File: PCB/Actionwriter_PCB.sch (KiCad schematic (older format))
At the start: 20 parts, among them J1 Conn_01x01, U1 74HC595, U2 74HC595

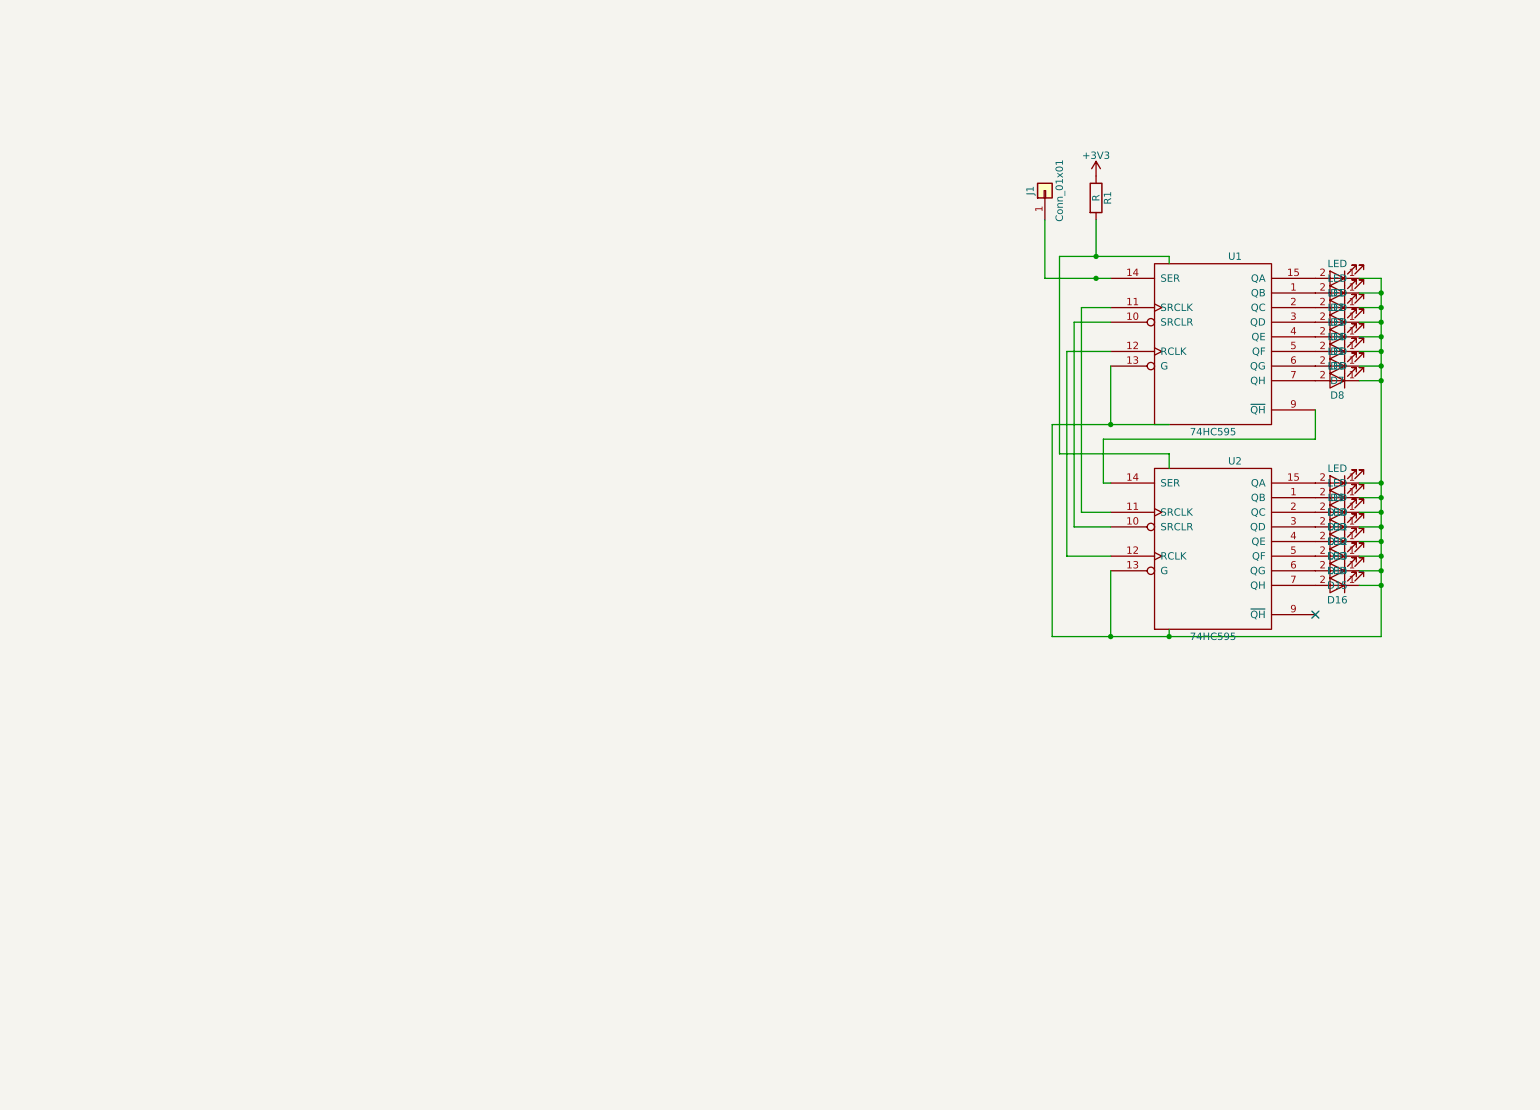
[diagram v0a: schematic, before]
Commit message: Schematic seems finished
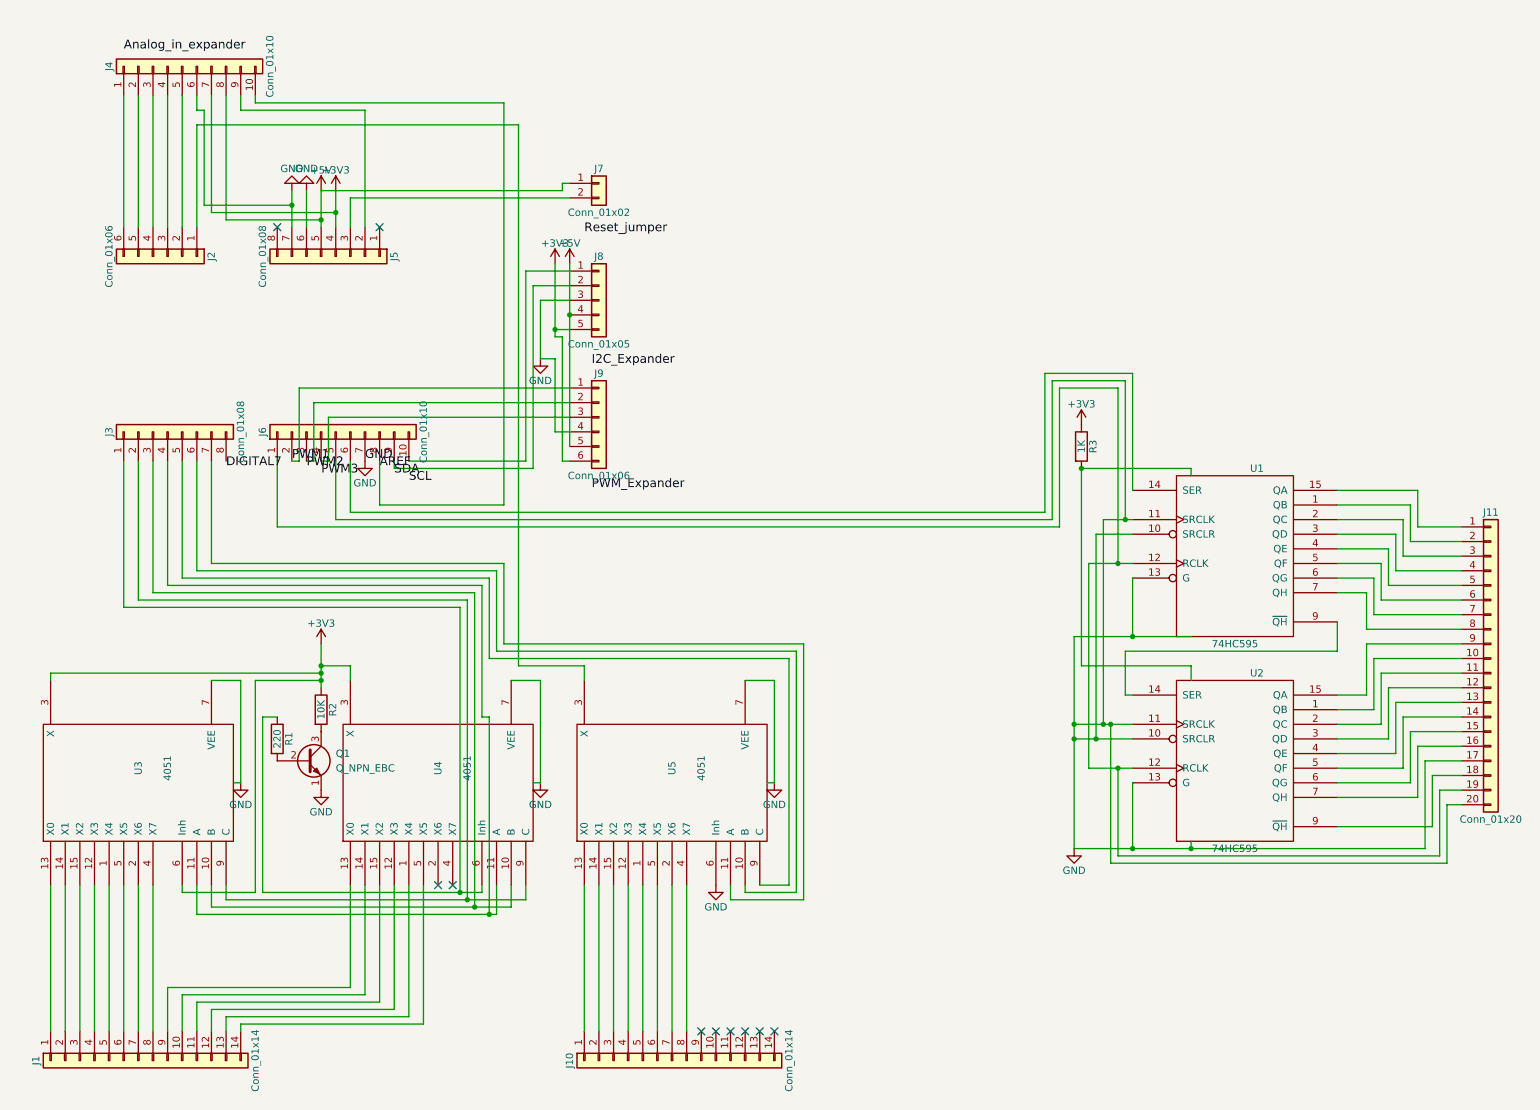
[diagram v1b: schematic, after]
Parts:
- removed D1, D10, D11, D12, D13, D14, D15, D16, D2, D3, D4, D5, D6, D7, D8, D9: LED, LEDs:LED_D5.0mm, symbol LED
- removed J1: Conn_01x01, Pin_Headers:Pin_Header_Straight_1x01_Pitch1.00mm, symbol Conn_01x01
- added J1, J10: Conn_01x14, Pin_Headers:Pin_Header_Straight_1x14_Pitch2.54mm, symbol Conn_01x14
- added J11: Conn_01x20, Pin_Headers:Pin_Header_Straight_1x20_Pitch2.54mm, symbol Conn_01x20
- added J2, J9: Conn_01x06, Pin_Headers:Pin_Header_Straight_1x06_Pitch2.54mm, symbol Conn_01x06
- added J3, J5: Conn_01x08, Pin_Headers:Pin_Header_Straight_1x08_Pitch2.54mm, symbol Conn_01x08
- added J4, J6: Conn_01x10, Pin_Headers:Pin_Header_Straight_1x10_Pitch2.54mm, symbol Conn_01x10
- added J7: Conn_01x02, Pin_Headers:Pin_Header_Straight_1x02_Pitch2.54mm, symbol Conn_01x02
- added J8: Conn_01x05, Pin_Headers:Pin_Header_Straight_1x05_Pitch2.54mm, symbol Conn_01x05
- added Q1: Q_NPN_EBC, Transistors_OldSowjetAera:OldSowjetaera_Transistor_Type-II_SmallPads, symbol Q_NPN_EBC
- added R2: 10K, Resistors_SMD:R_1206_HandSoldering, symbol R
- added R3: 1K, Resistors_SMD:R_1206_HandSoldering, symbol R
- added U3, U4, U5: 4051, Housings_DIP:DIP-16_W7.62mm, symbol 4051
- R1: value R -> 220; footprint Resistors_SMD:R_0805_HandSoldering -> Resistors_SMD:R_1206_HandSoldering
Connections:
- net +3V3: now also J4.7 (Pin_7), J5.4 (Pin_4), J8.5 (Pin_5), J9.6 (Pin_6), R2.1, R3.1, U3.3 (X), U3.6 (Inh), U4.3 (X); no longer R1.1
- net GND: now also U1.10 (SRCLR), U1.11 (SRCLK), U2.10 (SRCLR), U2.11 (SRCLK), J11.17 (Pin_17), J11.20 (Pin_20), J4.6 (Pin_6), J5.6 (Pin_6), J5.7 (Pin_7), J6.5 (Pin_5), J6.7 (Pin_7), J8.3 (Pin_3), J9.4 (Pin_4), Q1.1 (E), U3.7 (VEE), U3.8 (VSS), U4.7 (VEE), U4.8 (VSS), U5.6 (Inh), U5.7 (VEE), U5.8 (VSS)
- net VCC: now also R3.2; no longer R1.2
- net at U1.1 (QB): now also J11.2 (Pin_2)
- net at U1.12 (RCLK), U2.12 (RCLK): now also J11.19 (Pin_19), J6.1 (Pin_1)
- net at U1.14 (SER): now also J6.6 (Pin_6)
- net at U1.15 (QA): now also J11.1 (Pin_1)
- net at U1.2 (QC): now also J11.3 (Pin_3)
- net at U1.3 (QD): now also J11.4 (Pin_4)
- net at U1.4 (QE): now also J11.5 (Pin_5)
- net at U1.5 (QF): now also J11.6 (Pin_6)
- net at U1.6 (QG): now also J11.7 (Pin_7)
- net at U1.7 (QH): now also J11.8 (Pin_8)
- net at U2.1 (QB): now also J11.10 (Pin_10)
- net at U2.15 (QA): now also J11.9 (Pin_9)
- net at U2.2 (QC): now also J11.11 (Pin_11)
- net at U2.3 (QD): now also J11.12 (Pin_12)
- net at U2.4 (QE): now also J11.13 (Pin_13)
- net at U2.5 (QF): now also J11.14 (Pin_14)
- net at U2.6 (QG): now also J11.15 (Pin_15)
- net at U2.7 (QH): now also J11.16 (Pin_16)
- net at U2.9 (~QH): now also J11.18 (Pin_18)
- new net: J1.1 (Pin_1), U3.13 (X0)
- new net: J1.10 (Pin_10), U4.14 (X1)
- new net: J1.11 (Pin_11), U4.15 (X2)
- new net: J1.12 (Pin_12), U4.12 (X3)
- new net: J1.13 (Pin_13), U4.1 (X4)
- new net: J1.14 (Pin_14), U4.5 (X5)
- new net: J1.2 (Pin_2), U3.14 (X1)
- new net: J1.3 (Pin_3), U3.15 (X2)
- new net: J1.4 (Pin_4), U3.12 (X3)
- new net: J1.5 (Pin_5), U3.1 (X4)
- new net: J1.6 (Pin_6), U3.5 (X5)
- new net: J1.7 (Pin_7), U3.2 (X6)
- new net: J1.8 (Pin_8), U3.4 (X7)
- new net: J1.9 (Pin_9), U4.13 (X0)
- new net: J10.1 (Pin_1), U5.13 (X0)
- new net: J10.2 (Pin_2), U5.14 (X1)
- new net: J10.3 (Pin_3), U5.15 (X2)
- new net: J10.4 (Pin_4), U5.12 (X3)
- new net: J10.5 (Pin_5), U5.1 (X4)
- new net: J10.6 (Pin_6), U5.5 (X5)
- new net: J10.7 (Pin_7), U5.2 (X6)
- new net: J10.8 (Pin_8), U5.4 (X7)
- new net: J3.3 (Pin_3), U3.10 (B), U4.10 (B)
- new net: J3.4 (Pin_4), U3.11 (A), U4.11 (A)
- new net: J3.2 (Pin_2), U3.9 (C), U4.9 (C)
- new net: J3.1 (Pin_1), R1.1, U4.6 (Inh)
- new net: J3.6 (Pin_6), U5.10 (B)
- new net: J3.7 (Pin_7), U5.11 (A)
- new net: J2.1 (Pin_1), U5.3 (X)
- new net: J3.5 (Pin_5), U5.9 (C)
- new net: Q1.2 (B), R1.2
- new net: Q1.3 (C), R2.2
- new net: J6.10 (Pin_10), J8.1 (Pin_1)
- new net: J6.3 (Pin_3), J9.2 (Pin_2)
- new net: J6.4 (Pin_4), J9.3 (Pin_3)
- new net: J6.9 (Pin_9), J8.2 (Pin_2)
- new net: J4.9 (Pin_9), J5.2 (Pin_2)
- new net: J5.3 (Pin_3), J7.2 (Pin_2)
- new net: J2.2 (Pin_2), J4.5 (Pin_5)
- new net: J2.3 (Pin_3), J4.4 (Pin_4)
- new net: J2.4 (Pin_4), J4.3 (Pin_3)
- new net: J2.5 (Pin_5), J4.2 (Pin_2)
- new net: J2.6 (Pin_6), J4.1 (Pin_1)
- new net +5V: J4.8 (Pin_8), J5.5 (Pin_5), J7.1 (Pin_1), J8.4 (Pin_4), J9.5 (Pin_5)
- new net AREF: J4.10 (Pin_10), J6.8 (Pin_8)
- new net PWM1: J6.2 (Pin_2), J9.1 (Pin_1)
- new net VDD: U3.16 (VDD), U4.16 (VDD), U5.16 (VDD)
- no-connect marks 1 -> 10
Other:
- moved on the sheet: U1, U2

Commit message: Test moving some address lines to 0 and 1 (for later use of PWM), PCB work
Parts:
- removed J11: Conn_01x20, Pin_Headers:Pin_Header_Straight_1x20_Pitch2.54mm, symbol Conn_01x20
- removed J4: Conn_01x10, Pin_Headers:Pin_Header_Straight_1x10_Pitch2.54mm, symbol Conn_01x10
- removed Q1: Q_NPN_EBC, Transistors_OldSowjetAera:OldSowjetaera_Transistor_Type-II_SmallPads, symbol Q_NPN_EBC
- added J11: LEDS0, Pin_Headers:Pin_Header_Straight_1x09_Pitch2.54mm, symbol Conn_01x09
- added J12: LEDS1, Pin_Headers:Pin_Header_Straight_1x09_Pitch2.54mm, symbol Conn_01x09
- added J13: LEDX, Pin_Headers:Pin_Header_Straight_1x04_Pitch1.27mm_SMD_Pin1Right, symbol Conn_01x04
- added J4: AIN_D8_Expander, Pin_Headers:Pin_Header_Straight_1x11_Pitch2.54mm, symbol Conn_01x11
- added Q1: PN2222A, TO_SOT_Packages_THT:TO-92_Molded_Narrow, symbol PN2222A
- added Q2, Q3, Q4: IRLB8721PBF, TO_SOT_Packages_THT:TO-220-3_Vertical, symbol IRLB8721PBF
- J1: value Conn_01x14 -> KBD_LHS
- J10: value Conn_01x14 -> KBD_RHS; symbol Conn_01x14 -> Conn_01x16
- J2: value Conn_01x06 -> Arduino_AnalogIn
- J3: value Conn_01x08 -> Arduino_DigitalLow
- J5: value Conn_01x08 -> Arduino_power
- J6: value Conn_01x10 -> Arduino_DigitalHigh
- J7: value Conn_01x02 -> Reset_Jumper; footprint Pin_Headers:Pin_Header_Straight_1x02_Pitch2.54mm -> Pin_Headers:Pin_Header_Straight_1x03_Pitch2.54mm; symbol Conn_01x02 -> Conn_01x03
- J8: value Conn_01x05 -> I2C_Expander
- J9: value Conn_01x06 -> RGB_Expander
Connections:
- net VCC is gone; now on net +3V3: R3.2, U1.16 (VCC), U2.16 (VCC)
- net VDD is gone; now on net +3V3: U3.16 (VDD), U4.16 (VDD), U5.16 (VDD)
- net +3V3: now also J9.5 (Pin_5), J4.8 (Pin_8); no longer J9.6 (Pin_6)
- net +5V: now also J9.6 (Pin_6), J4.7 (Pin_7); no longer J7.1 (Pin_1), J9.5 (Pin_5)
- net AREF: now also J4.10 (Pin_10)
- net DIGITAL7: now also J3.8 (Pin_8), J4.11 (Pin_11)
- net GND: now also J7.1 (Pin_1), J11.1 (Pin_1), J12.9 (Pin_9), J13.2 (Pin_2), J13.4 (Pin_4), J4.6 (Pin_6), Q1.1 (E), Q2.3 (S), Q3.3 (S), Q4.3 (S); no longer J9.4 (Pin_4)
- net PWM1: now also Q2.1 (G); no longer J9.1 (Pin_1)
- net PWM2: now also J6.3 (Pin_3), Q3.1 (G)
- net PWM3: now also J6.4 (Pin_4), Q4.1 (G)
- net SCL: now also J6.10 (Pin_10), J8.1 (Pin_1)
- net SDA: now also J6.9 (Pin_9), J8.2 (Pin_2)
- net at U1.1 (QB): now also J11.3 (Pin_3)
- net at J6.1 (Pin_1), U1.12 (RCLK), U2.12 (RCLK): now also J13.3 (Pin_3)
- net at U1.15 (QA): now also J11.2 (Pin_2)
- net at U1.2 (QC): now also J11.4 (Pin_4)
- net at U1.3 (QD): now also J11.5 (Pin_5)
- net at U1.4 (QE): now also J11.6 (Pin_6)
- net at U1.5 (QF): now also J11.7 (Pin_7)
- net at U1.6 (QG): now also J11.8 (Pin_8)
- net at U1.7 (QH): now also J11.9 (Pin_9)
- net at U2.1 (QB): now also J12.2 (Pin_2)
- net at U2.15 (QA): now also J12.1 (Pin_1)
- net at U2.2 (QC): now also J12.3 (Pin_3)
- net at U2.3 (QD): now also J12.4 (Pin_4)
- net at U2.4 (QE): now also J12.5 (Pin_5)
- net at U2.5 (QF): now also J12.6 (Pin_6)
- net at U2.6 (QG): now also J12.7 (Pin_7)
- net at U2.7 (QH): now also J12.8 (Pin_8)
- net at U2.9 (~QH): now also J13.1 (Pin_1)
- net at R1.2: now also Q1.2 (B)
- net at R2.2: now also Q1.3 (C)
- net at J9.2 (Pin_2): now also Q3.2 (D); no longer J6.3 (Pin_3)
- net at J9.3 (Pin_3): now also Q4.2 (D); no longer J6.4 (Pin_4)
- net at J5.2 (Pin_2): now also J4.9 (Pin_9)
- net at J5.8 (Pin_8): now also J9.4 (Pin_4)
- net at J2.2 (Pin_2): now also J7.3 (Pin_3), J4.5 (Pin_5)
- net at J2.3 (Pin_3): now also J4.4 (Pin_4)
- net at J2.4 (Pin_4): now also J4.3 (Pin_3)
- net at J2.5 (Pin_5): now also J4.2 (Pin_2)
- net at J2.6 (Pin_6): now also J4.1 (Pin_1)
- new net: J9.1 (Pin_1), Q2.2 (D)
- no-connect marks 10 -> 11

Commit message: updated?
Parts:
- J10: footprint Pin_Headers:Pin_Header_Straight_1x14_Pitch2.54mm -> Pin_Headers:Pin_Header_Straight_1x16_Pitch2.54mm
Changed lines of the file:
@@
 F 0 "J10" H 5100 8250 50  0000 C CNN
 F 1 "KBD_RHS" H 5100 6550 50  0000 C CNN
-F 2 "Pin_Headers:Pin_Header_Straight_1x14_Pitch2.54mm" H 5100 7450 50  0001 C CNN
+F 2 "Pin_Headers:Pin_Header_Straight_1x16_Pitch2.54mm" H 5100 7450 50  0001 C CNN
 F 3 "" H 5100 7450 50  0001 C CNN
 	1    5100 7450
